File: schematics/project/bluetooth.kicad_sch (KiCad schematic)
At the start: 0 parts

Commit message: First steps with kicad structure -> kinda sucks
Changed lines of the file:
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@@
 (kicad_sch (version 20211123) (generator eeschema)
   (paper "A4")
-  (hierarchical_label "bt_tx" (shape input) (at 200.66 44.45 0)
+  (hierarchical_label "bt_tx" (shape input) (at 120.65 85.09 0)
     (effects (font (size 1.27 1.27)) (justify left))
   )
-  (hierarchical_label "bt_rx" (shape output) (at 200.66 52.07 0)
+  (hierarchical_label "bt_rx" (shape output) (at 120.65 87.63 0)
     (effects (font (size 1.27 1.27)) (justify left))
   )

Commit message: some progress, dust slowly clears
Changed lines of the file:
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@@
 (kicad_sch (version 20211123) (generator eeschema)
   (paper "A4")
-  (hierarchical_label "bt_tx" (shape input) (at 120.65 85.09 0)
-    (effects (font (size 1.27 1.27)) (justify left))
+  (bus_alias "Bluetooth" (members "BT_rx" "BT_tx"))
+  (bus_entry (at 69.85 52.07) (size 2.54 2.54)
+    (stroke (width 0) (type default) (color 0 0 0 0))
   )
-  (hierarchical_label "bt_rx" (shape output) (at 120.65 87.63 0)
-    (effects (font (size 1.27 1.27)) (justify left))
+  (bus_entry (at 69.85 54.61) (size 2.54 2.54)
+    (stroke (width 0) (type default) (color 0 0 0 0))
+  )
+  (wire (pts (xy 72.39 54.61) (xy 81.28 54.61))
+    (stroke (width 0) (type default) (color 0 0 0 0))
+  )
+  (wire (pts (xy 72.39 57.15) (xy 81.28 57.15))
+    (stroke (width 0) (type default) (color 0 0 0 0))
+  )
+  (bus (pts (xy 69.85 52.07) (xy 69.85 54.61))
+    (stroke (width 0) (type default) (color 0 0 0 0))
+  )
+  (bus (pts (xy 54.61 52.07) (xy 69.85 52.07))
+    (stroke (width 0) (type default) (color 0 0 0 0))
+  )
+  (label "BT_rx" (at 81.28 57.15 0)
+    (effects (font (size 1.27 1.27)) (justify left bottom))
+  )
+  (label "BT_tx" (at 81.28 54.61 0)
+    (effects (font (size 1.27 1.27)) (justify left bottom))
+  )
+  (label "{Bluetooth}" (at 57.15 52.07 0)
+    (effects (font (size 1.27 1.27)) (justify left bottom))
+  )
+  (hierarchical_label "Bluetooth" (shape bidirectional) (at 54.61 52.07 180)
+    (effects (font (size 1.27 1.27)) (justify right))
   )
 )

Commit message: small progress, angsthasen
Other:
- note added: "5V mabye"
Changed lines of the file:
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@@
     (stroke (width 0) (type default) (color 0 0 0 0))
+  )
+  (text "5V mabye\n" (at 114.3 48.26 0)
+    (effects (font (size 1.27 1.27)) (justify left bottom))
   )
   (label "BT_rx" (at 81.28 57.15 0)

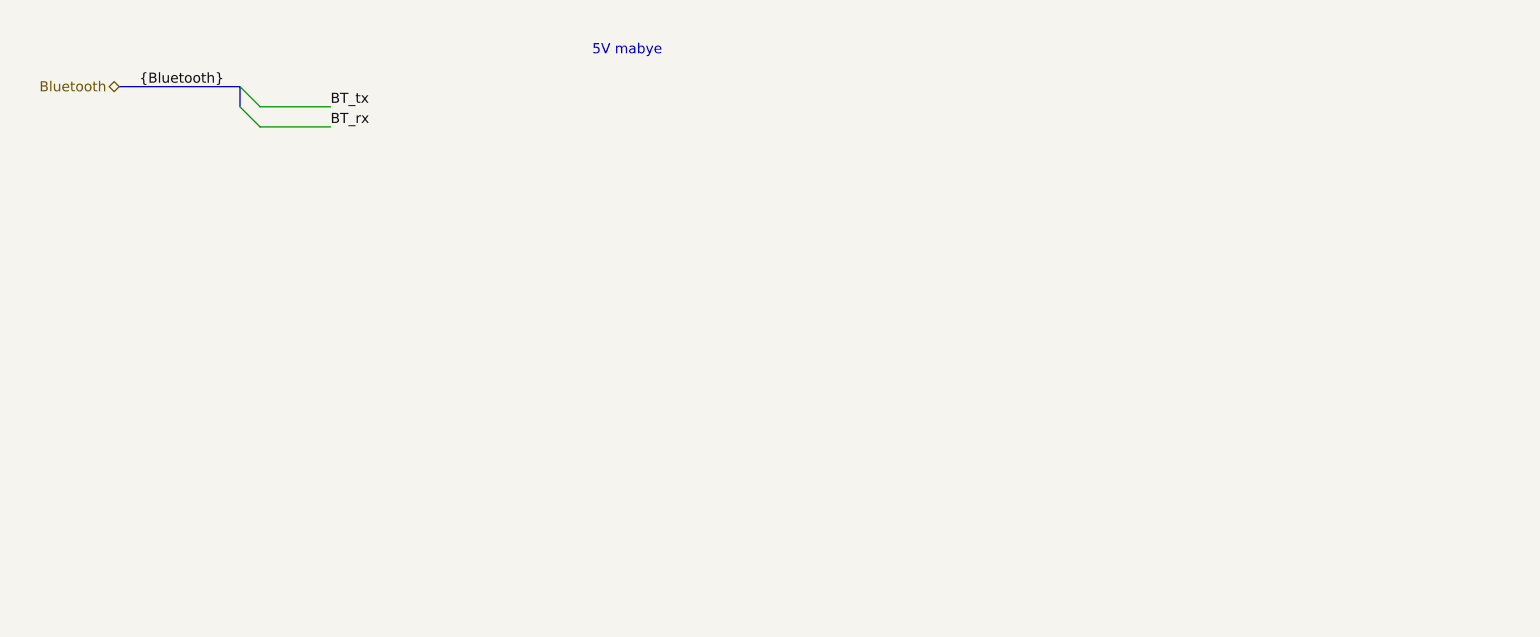
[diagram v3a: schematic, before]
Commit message: Adding separate library, BT Module
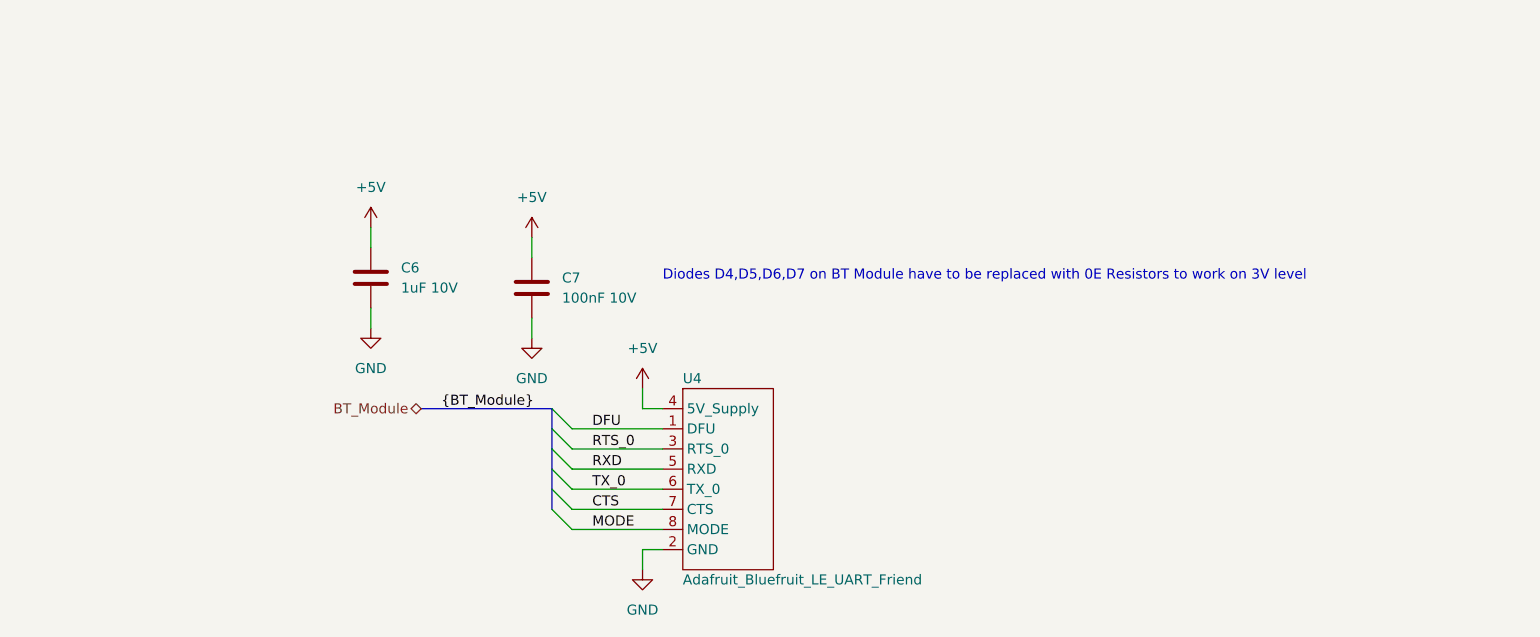
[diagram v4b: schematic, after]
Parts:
- added C6: 1uF 10V, Capacitor_SMD:C_0603_1608Metric, symbol Device:C
- added C7: 100nF 10V, Capacitor_SMD:C_0603_1608Metric, symbol Device:C
- added U4: Adafruit_Bluefruit_LE_UART_Friend, IceWheelLib:Adafruit_Bluefruit_LE_UART_Friend, symbol IceWheelLib:Adafruit_Bluefruit_LE_UART_Friend
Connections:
- new net +5V: C6.1, C7.1, U4.4 (5V_Supply)
- new net CTS: U4.7 (CTS)
- new net DFU: U4.1 (DFU)
- new net GND: C6.2, C7.2, U4.2 (GND)
- new net MODE: U4.8 (MODE)
- new net RTS_0: U4.3 (RTS_0)
- new net RXD: U4.5 (RXD)
- new net TX_0: U4.6 (TX_0)
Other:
- note added: "Diodes D4,D5,D6,D7 on BT Module have to be replaced with 0E Resistors to work on 3V level"
- note removed: "5V mabye"
